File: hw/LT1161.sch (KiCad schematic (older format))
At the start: 6 parts, among them U401 MOSFET_DRIVER_LT1161, U402 MOSFET_IPG20N04S4L11ATMA1, U403 MOSFET_IPG20N04S4L11ATMA1

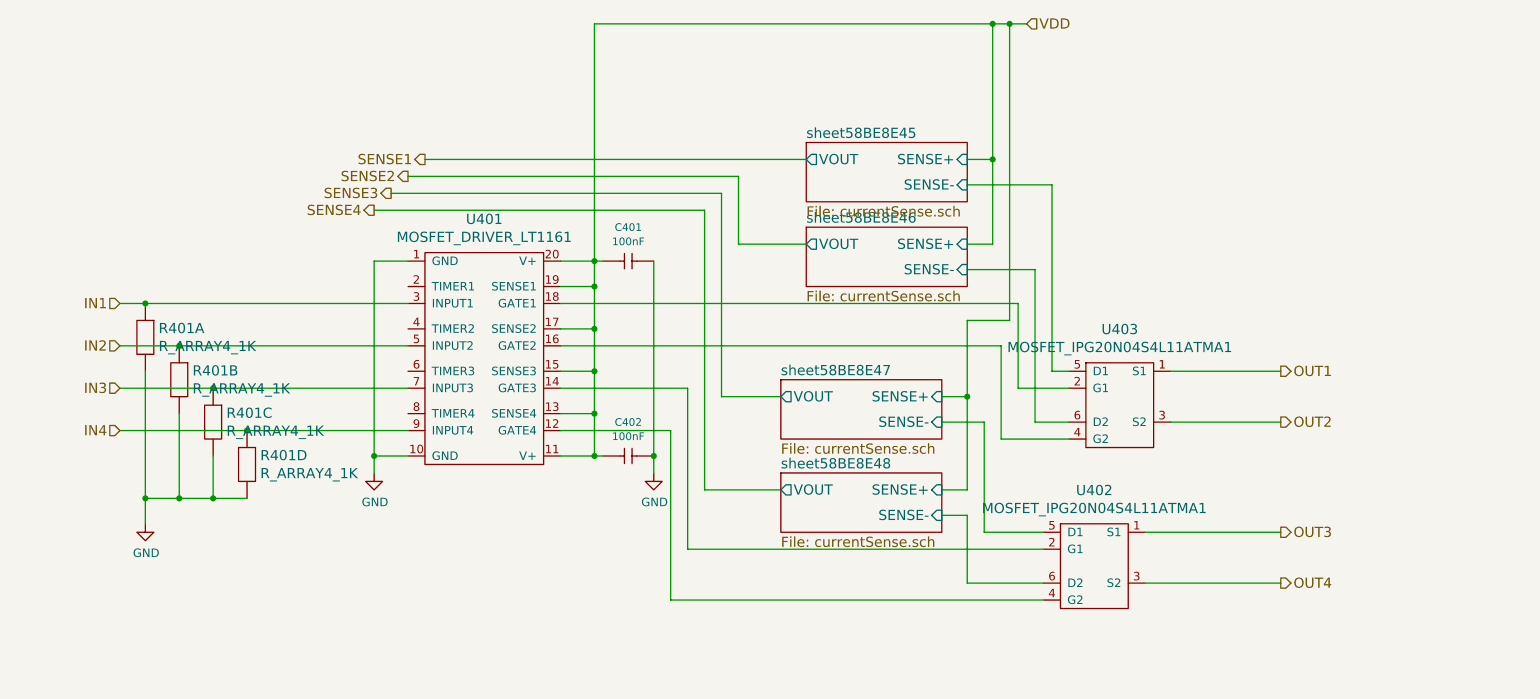
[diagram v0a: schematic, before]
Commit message: at least shortcirucuit protection works
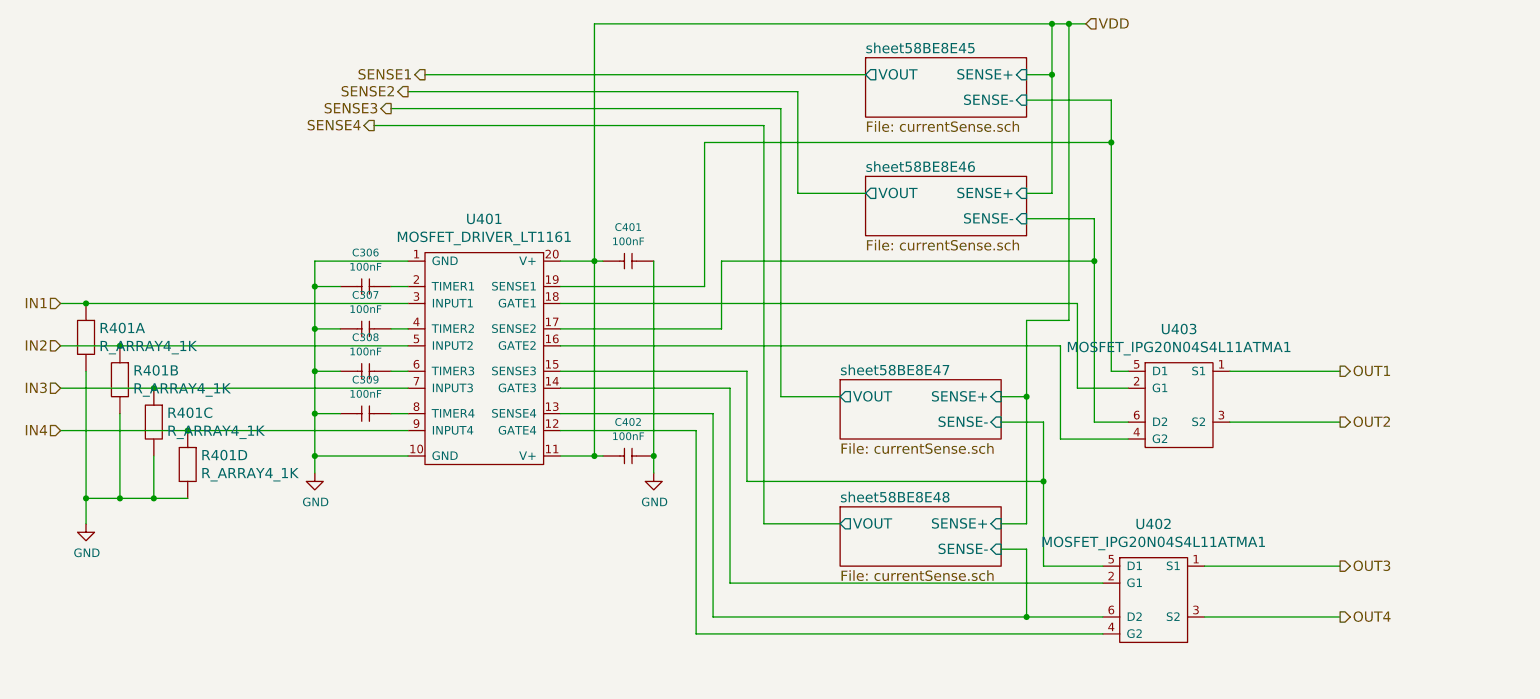
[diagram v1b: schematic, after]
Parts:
- added C306, C307, C308, C309: 100nF, kemet:0603, symbol 100nF
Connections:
- net GND: now also C306.1 (C1), C307.1 (C1), C308.1 (C1), C309.1 (C1)
- net VDD: no longer U401.13 (SENSE4), U401.15 (SENSE3), U401.17 (SENSE2), U401.19 (SENSE1)
- net sheet58BE8E45/SENSE-: now also U401.19 (SENSE1)
- net sheet58BE8E46/SENSE-: now also U401.17 (SENSE2)
- net sheet58BE8E47/SENSE-: now also U401.15 (SENSE3)
- net sheet58BE8E48/SENSE-: now also U401.13 (SENSE4)
- net at U401.2 (TIMER1): now also C306.2 (C2)
- net at U401.4 (TIMER2): now also C307.2 (C2)
- net at U401.6 (TIMER3): now also C308.2 (C2)
- net at U401.8 (TIMER4): now also C309.2 (C2)
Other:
- moved on the sheet: R401A, R401B, R401C, R401D, U402, U403

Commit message: starting to draw version 4.0.0
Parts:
- removed U402: MOSFET_IPG20N04S4L11ATMA1, usevolt:PG-TDSON-8-4, symbol MOSFET_IPG20N04S4L11ATMA1
- added U302, U304: MOSFET_IPG20N04S4L11ATMA1, usevolt:PG-TDSON-8-4, symbol MOSFET_IPG20N04S4L11ATMA1
- renumbered C306 to C301, C307 to C302, C308 to C303, C309 to C304, C401 to C305, C402 to C306, R401 to R301, U401 to U301, U403 to U303
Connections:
- net OUT1: now also U303.3 (S2); no longer U303.1 (S1)
- net OUT2: now also U304.1 (S1), U304.3 (S2); no longer U303.3 (S2)
- net OUT3: now also U303.1 (S1)
- net OUT4: now also U302.1 (S1), U302.3 (S2)
- net sheet58BE8E45/SENSE-: now also U303.6 (D2); no longer U303.5 (D1)
- net sheet58BE8E46/SENSE-: now also U304.5 (D1), U304.6 (D2); no longer U303.6 (D2)
- net sheet58BE8E47/SENSE-: now also U303.5 (D1)
- net sheet58BE8E48/SENSE-: now also U302.5 (D1), U302.6 (D2)
- net at U303.2 (G1): now also U301.14 (GATE3); no longer U301.18 (GATE1)
- net at U303.4 (G2): now also U301.18 (GATE1); no longer U301.16 (GATE2)
- net at U301.12 (GATE4): now also U302.2 (G1), U302.4 (G2)
- new net: U301.16 (GATE2), U304.2 (G1), U304.4 (G2)
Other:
- moved on the sheet: U303
